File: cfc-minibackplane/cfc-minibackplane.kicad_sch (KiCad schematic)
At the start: 33 parts, among them J1 m55-6001642, J2 Harwin M80-5400442, J3 PI 1792627 + PI 1861690, J4 ORESAT-DEBUG-CONNECTOR-ALL, U2 AMS1117-3.3

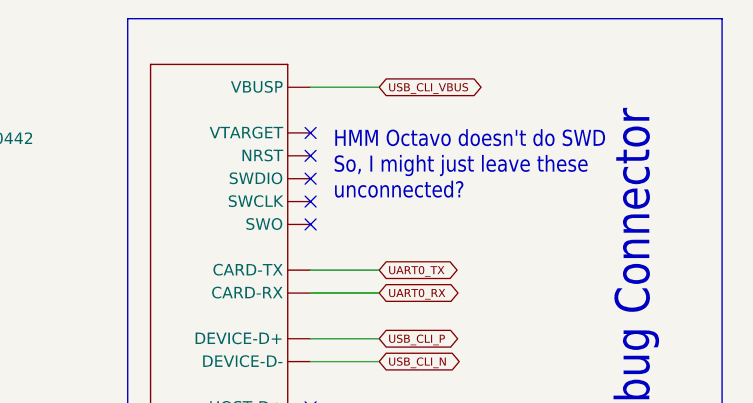
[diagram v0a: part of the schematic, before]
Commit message: Updated 3d models
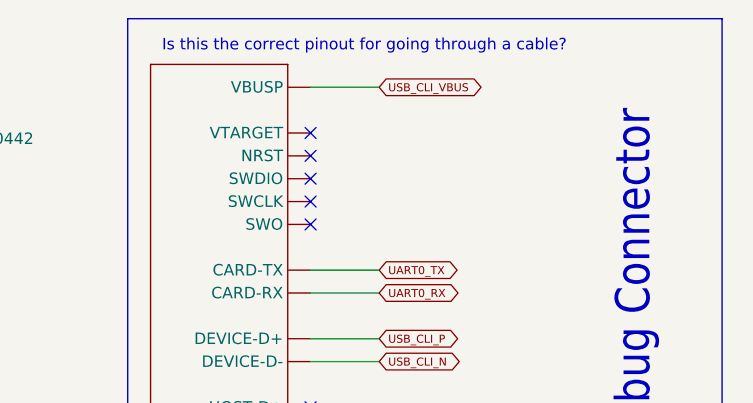
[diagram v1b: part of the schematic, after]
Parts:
- C1.1, C1.2, C20.1, C20.2: footprint oresat-passives:0603-SMALL -> Capacitor_SMD:C_0603_1608Metric
- R1.1, R1.2, R1.3, R1.4, R2, R20.1, R20.2, R20.3, R20.4, R20.5, R20.6, R3: footprint oresat-passives:0603-SMALL -> Resistor_SMD:R_0603_1608Metric
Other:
- note added: "Is this the correct pinout for going through a cable?"
- note removed: "HMM Octavo doesn't do SWD So, I might just leave these unconnected?"
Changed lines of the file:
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@@
+    (effects (font (size 1.27 1.27)) (justify left bottom))
+  )
+  (text "Is this the correct pinout for going through a cable?"
+    (at 350.52 26.67 0)
     (effects (font (size 1.27 1.27)) (justify left bottom))
   )
@@
   (text "Oresat Debug Connector" (at 405.13 33.02 90)
     (effects (font (size 3.81 3.2385)) (justify right bottom))
-  )
-  (text "HMM Octavo doesn't do SWD\nSo, I might just leave these\nunconnected?"
-    (at 369.57 43.18 0)
-    (effects (font (size 1.778 1.5113)) (justify left bottom))
   )
   (text "Aux connectors" (at 311.15 132.08 0)
@@
       (effects (font (size 1.778 1.5113)) (justify left bottom))
     )
-    (property "Footprint" "oresat-passives:0603-SMALL" (at 204.47 125.73 90)
+    (property "Footprint" "Resistor_SMD:R_0603_1608Metric" (at 204.47 125.73 90)
       (effects (font (size 1.27 1.27)) hide)
     )
@@
       (effects (font (size 1.778 1.5113)) (justify left bottom))
     )
-    (property "Footprint" "oresat-passives:0603-SMALL" (at 269.24 171.45 90)
+    (property "Footprint" "Resistor_SMD:R_0603_1608Metric" (at 269.24 171.45 90)
       (effects (font (size 1.27 1.27)) hide)
     )
@@
       (effects (font (size 1.778 1.5113)) (justify left bottom))
     )
-    (property "Footprint" "oresat-passives:0603-SMALL" (at 276.86 180.34 0)
+    (property "Footprint" "Capacitor_SMD:C_0603_1608Metric" (at 276.86 180.34 0)
       (effects (font (size 1.27 1.27)) hide)
     )
@@
       (effects (font (size 1.778 1.5113)) (justify left bottom))
     )
-    (property "Footprint" "oresat-passives:0603-SMALL" (at 204.47 130.81 90)
+    (property "Footprint" "Resistor_SMD:R_0603_1608Metric" (at 204.47 130.81 90)
       (effects (font (size 1.27 1.27)) hide)
     )
@@
       (effects (font (size 1.778 1.5113)) (justify left bottom))
     )
-    (property "Footprint" "oresat-passives:0603-SMALL" (at 217.17 134.62 0)
+    (property "Footprint" "Capacitor_SMD:C_0603_1608Metric" (at 217.17 134.62 0)
       (effects (font (size 1.27 1.27)) hide)
     )
@@
       (effects (font (size 1.27 1.27)))
     )
-    (property "Footprint" "oresat-passives:0603-SMALL" (at 71.12 123.698 90)
+    (property "Footprint" "Resistor_SMD:R_0603_1608Metric" (at 71.12 123.698 90)
       (effects (font (size 1.27 1.27)) hide)
     )
@@
       (effects (font (size 1.778 1.5113)) (justify left bottom))
     )
-    (property "Footprint" "oresat-passives:0603-SMALL" (at 269.24 166.37 90)
+    (property "Footprint" "Resistor_SMD:R_0603_1608Metric" (at 269.24 166.37 90)
       (effects (font (size 1.27 1.27)) hide)
     )
@@
       (effects (font (size 1.778 1.5113)) (justify left bottom))
     )
-    (property "Footprint" "oresat-passives:0603-SMALL" (at 264.16 194.31 90)
+    (property "Footprint" "Resistor_SMD:R_0603_1608Metric" (at 264.16 194.31 90)
       (effects (font (size 1.27 1.27)) hide)
     )
@@
       (effects (font (size 1.778 1.5113)) (justify left bottom))
     )
-    (property "Footprint" "oresat-passives:0603-SMALL" (at 269.24 130.81 90)
+    (property "Footprint" "Resistor_SMD:R_0603_1608Metric" (at 269.24 130.81 90)
       (effects (font (size 1.27 1.27)) hide)
     )
@@
       (effects (font (size 1.778 1.5113)) (justify left bottom))
     )
-    (property "Footprint" "oresat-passives:0603-SMALL" (at 207.01 166.37 90)
+    (property "Footprint" "Resistor_SMD:R_0603_1608Metric" (at 207.01 166.37 90)
       (effects (font (size 1.27 1.27)) hide)
     )
@@
       (effects (font (size 1.778 1.5113)) (justify left bottom))
     )
-    (property "Footprint" "oresat-passives:0603-SMALL" (at 264.16 201.93 90)
+    (property "Footprint" "Resistor_SMD:R_0603_1608Metric" (at 264.16 201.93 90)
       (effects (font (size 1.27 1.27)) hide)
     )
@@
       (effects (font (size 1.778 1.5113)) (justify left bottom))
     )
-    (property "Footprint" "oresat-passives:0603-SMALL" (at 276.86 138.43 0)
+    (property "Footprint" "Capacitor_SMD:C_0603_1608Metric" (at 276.86 138.43 0)
       (effects (font (size 1.27 1.27)) hide)
     )
@@
       (effects (font (size 1.778 1.5113)) (justify left bottom))
     )
-    (property "Footprint" "oresat-passives:0603-SMALL" (at 207.01 171.45 90)
+    (property "Footprint" "Resistor_SMD:R_0603_1608Metric" (at 207.01 171.45 90)
       (effects (font (size 1.27 1.27)) hide)
     )
@@
       (effects (font (size 1.778 1.5113)) (justify left bottom))
     )
-    (property "Footprint" "oresat-passives:0603-SMALL" (at 269.24 125.73 90)
+    (property "Footprint" "Resistor_SMD:R_0603_1608Metric" (at 269.24 125.73 90)
       (effects (font (size 1.27 1.27)) hide)
     )
@@
       (effects (font (size 1.27 1.27)))
     )
-    (property "Footprint" "oresat-passives:0603-SMALL" (at 71.12 126.238 90)
+    (property "Footprint" "Resistor_SMD:R_0603_1608Metric" (at 71.12 126.238 90)
       (effects (font (size 1.27 1.27)) hide)
     )
@@
       (effects (font (size 1.778 1.5113)) (justify left bottom))
     )
-    (property "Footprint" "oresat-passives:0603-SMALL" (at 219.71 175.26 0)
-      (effects (font (size 1.27 1.27)) hide)
-    )
+    (property "Footprint" "Capacitor_SMD:C_0603_1608Metric" (at 219.71 175.26 0)
+      (effects (font (size 1.27 1.27)) hide)
+    )

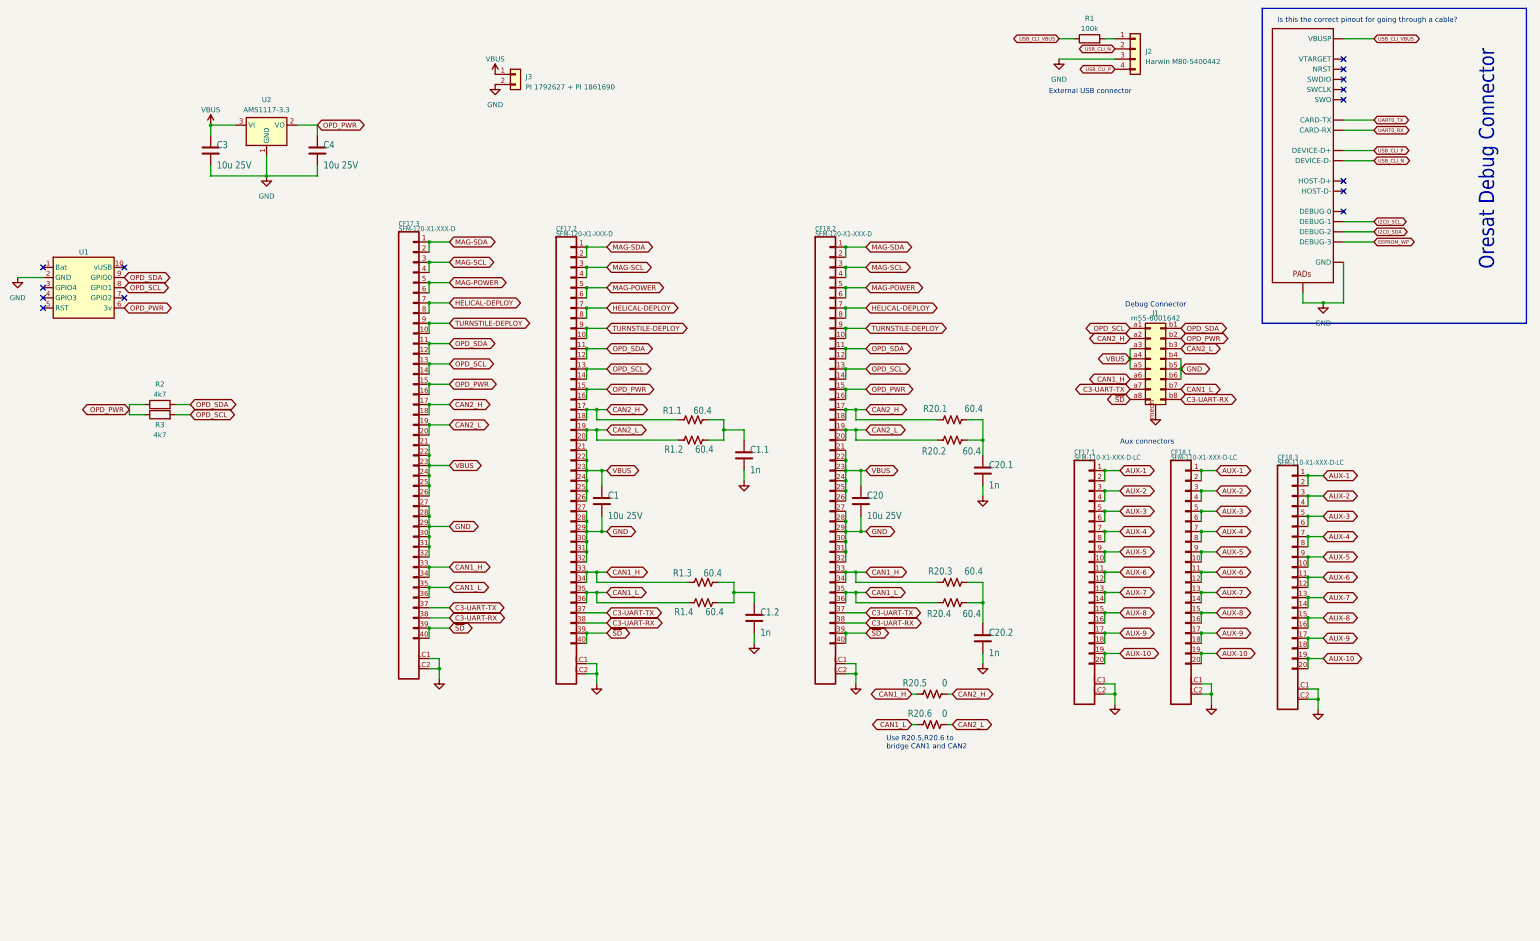
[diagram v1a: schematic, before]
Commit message: Cleaned up schematic and silkscreen
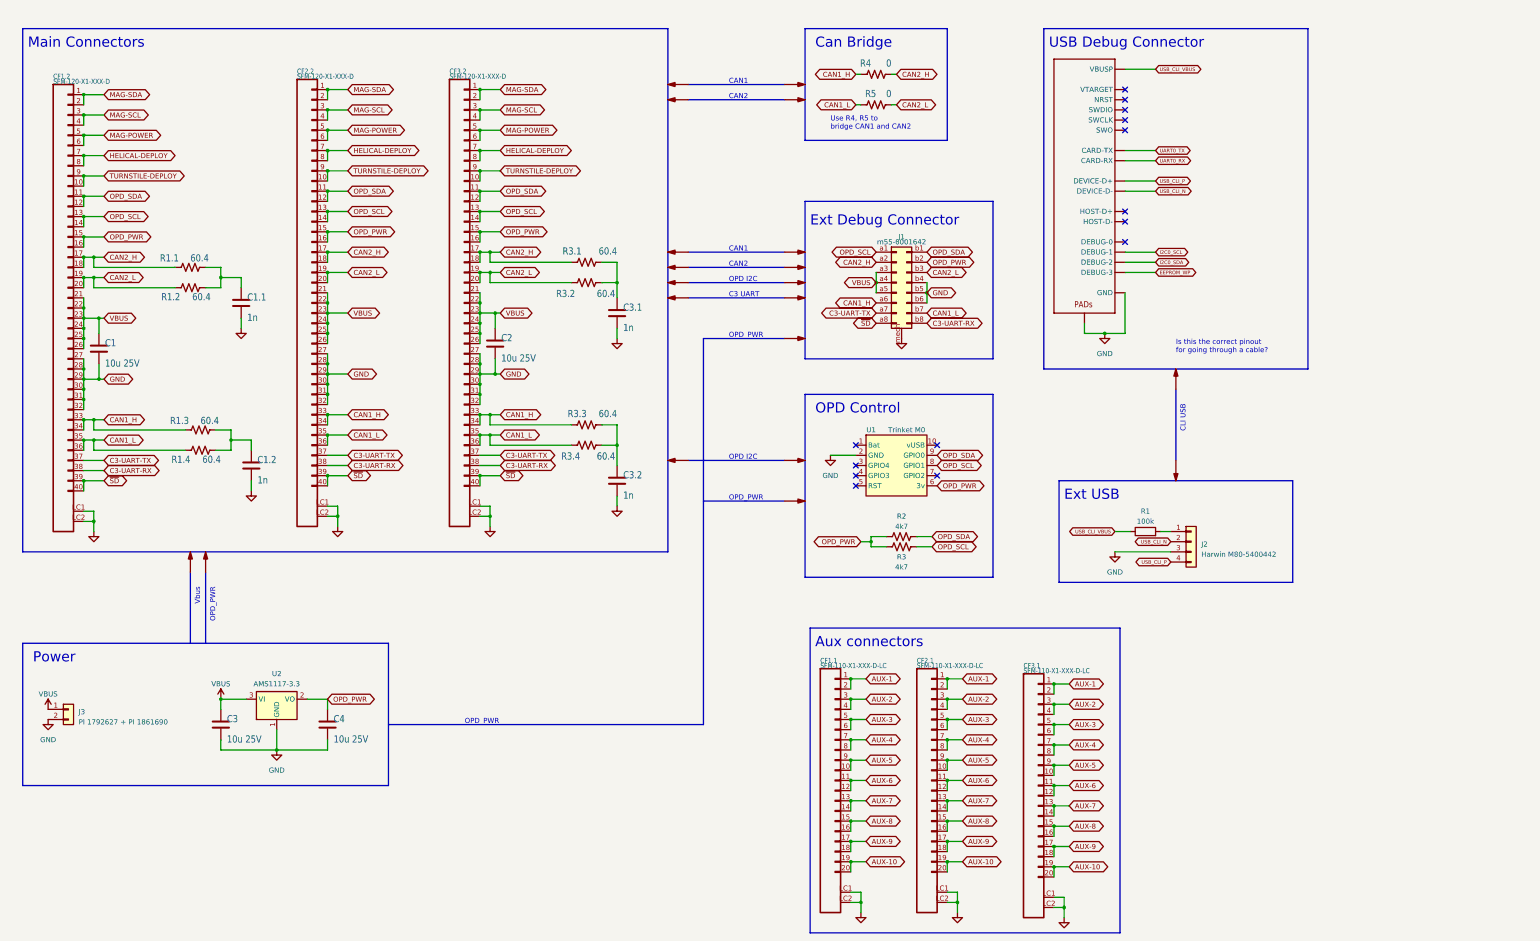
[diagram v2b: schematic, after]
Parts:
- R2, R3: symbol Device:R -> Device:R_US
- U1: value ~ -> Trinket M0
- renumbered C20 to C2, C20.1 to C3.1, C20.2 to C3.2, CF17.1 to CF1.1, CF17.2 to CF1.2, CF18.1 to CF2.1, CF17.3 to CF2.2, CF18.3 to CF3.1, CF18.2 to CF3.2, R20.1 to R3.1, R20.2 to R3.2, R20.3 to R3.3, R20.4 to R3.4, R20.5 to R4, R20.6 to R5
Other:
- note added: "C3 UART"
- note added: "CAN1"
- note added: "CAN2"
- note added: "CLI USB"
- note added: "Can Bridge"
- note added: "Ext Debug Connector"
- note added: "Ext USB"
- note added: "Main Connectors"
- note added: "OPD Control"
- note added: "OPD I2C"
- note added: "OPD_PWR"
- note added: "Power"
- note added: "USB Debug Connector"
- note added: "Use R4, R5 to bridge CAN1 and CAN2"
- note added: "Vbus"
- note removed: "Debug Connector"
- note removed: "External USB connector"
- note removed: "Oresat Debug Connector"
- note removed: "Use R20.5,R20.6 to bridge CAN1 and CAN2"
- title: (none) -> OreSat Mini Backplane
- moved on the sheet: C1, C1.1, C1.2, C2, C3, C3.1, C3.2, C4, CF1.1, CF1.2, CF2.1, CF2.2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

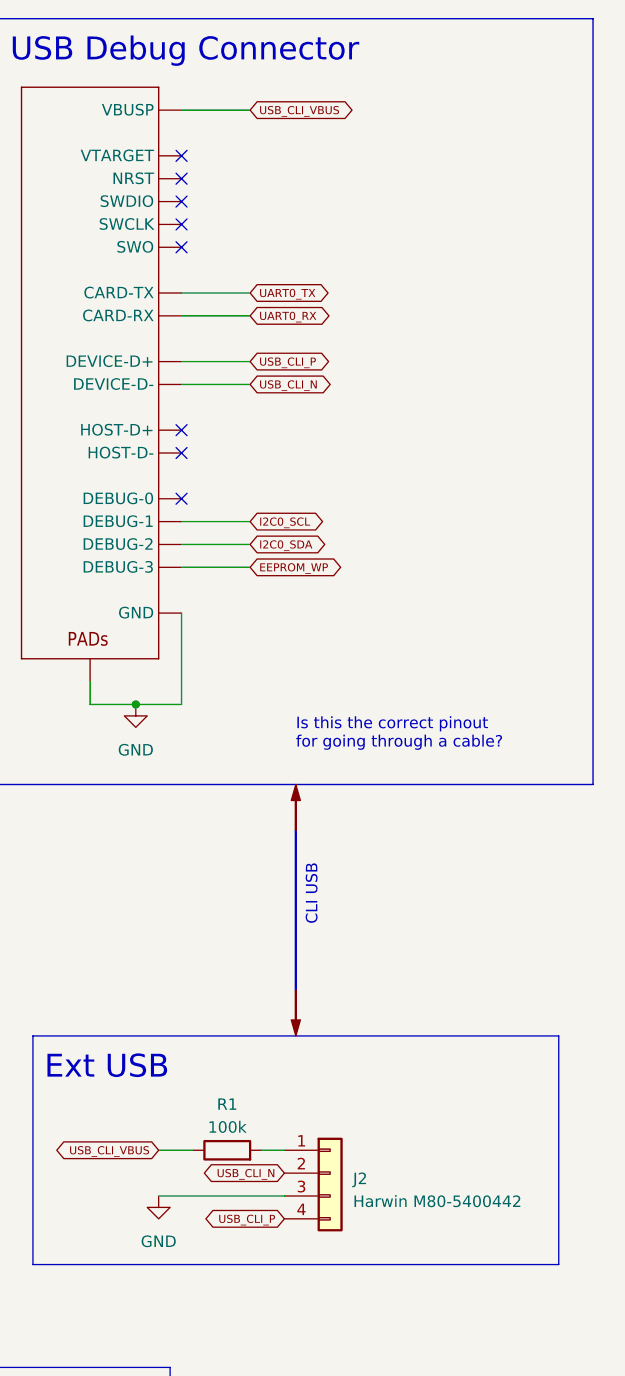
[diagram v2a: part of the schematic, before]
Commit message: Updated board based on CFC meeting
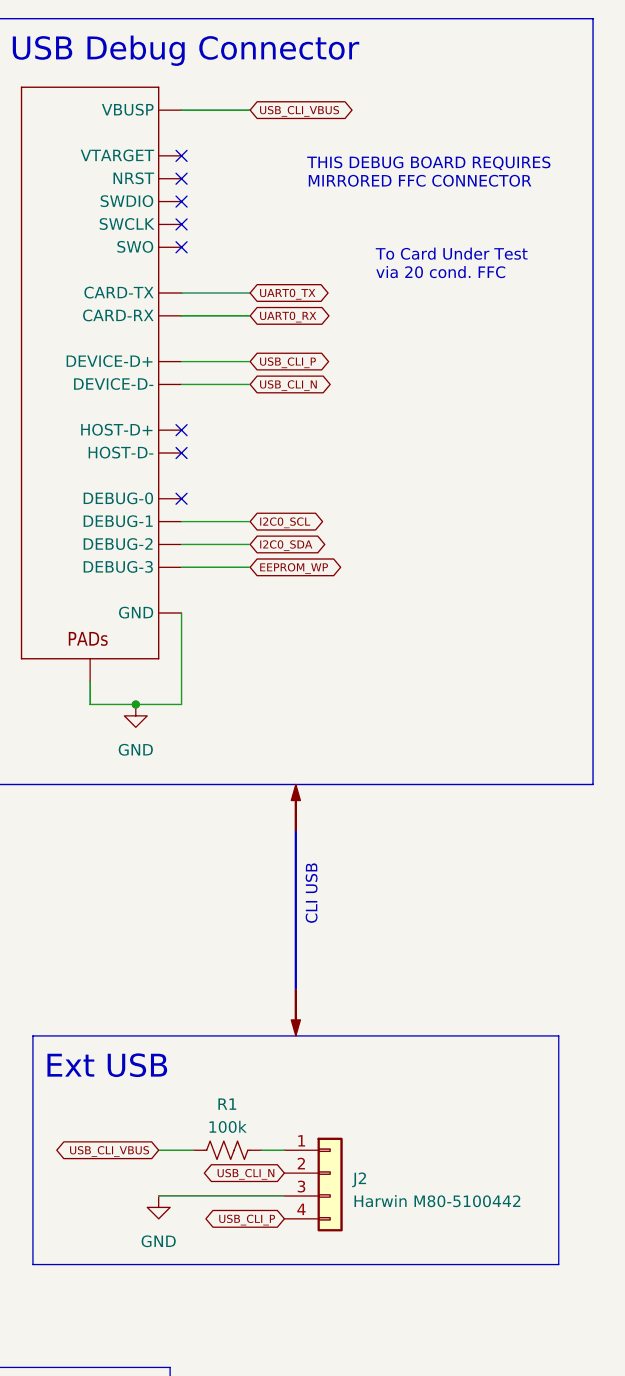
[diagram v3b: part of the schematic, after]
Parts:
- J2: value Harwin M80-5400442 -> Harwin M80-5100442; footprint oresat-connectors:J-Harwin-M80-5400442 -> oresat-connectors:J-Harwin-M80-5100442; DPN (none) -> 952-2343-ND; MPN (none) -> M80-5100442
- J3: footprint Connector_Phoenix_MSTB:PhoenixContact_MSTB_2,5_2-GF-5,08_1x02_P5.08mm_Horizontal_ThreadedFlange_MountHole -> Connector_Phoenix_MSTB:PhoenixContact_MSTBV_2,5_2-GF_1x02_P5.00mm_Vertical_ThreadedFlange_MountHole
- J4: footprint oresat-connectors:J-TE_2-1734592-0 -> oresat-connectors:J-TE_2-1734592-0_FFC_MIRRORED
- R1: footprint Resistor_SMD:R_1206_3216Metric -> Resistor_SMD:R_0603_1608Metric; symbol Device:R -> Device:R_US
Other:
- note added: "THIS DEBUG BOARD REQUIRES MIRRORED FFC CONNECTOR"
- note added: "To Card Under Test via 20 cond. FFC"
- note removed: "Is this the correct pinout for going through a cable?"

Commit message: Updated BOM
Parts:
- added J3.1: PC 1861690, symbol Graphic:SYM_Flash_Small
- C1, C2, C3, C4: DPN (none) -> GCM31CC71E106KA03K; MPN (none) -> 490-14533-1-ND
- C1.1, C1.2, C3.1, C3.2: DPN (none) -> 399-C0603C102F1GACAUTOCT-ND; MPN (none) -> GCM1885C2A102JA16D
- CF1.1, CF2.1, CF3.1: DPN (none) -> SFM-110-01-L-D-LC-ND; MPN (none) -> SFM-110-01-L-D-LC
- CF1.2, CF2.2, CF3.2: DPN (none) -> SFM-120-01-L-D-LC-ND; MPN (none) -> SFM-120-01-L-D-LC
- J1: DPN (none) -> M55-6001642R; MPN (none) -> 952-3836-1-ND
- J3: value PI 1792627 + PI 1861690 -> PC 180926; DPN (none) -> 277-2619-ND; MPN (none) -> 1809267
- J4: DPN (none) -> A100287CT-ND; MPN (none) -> 2-1734592-0
- R1: DPN (none) -> RHM100KAFCT-ND; MPN (none) -> ESR18EZPF1003
- R1.1, R1.2, R1.3, R1.4, R3.1, R3.2, R3.3, R3.4: footprint Resistor_SMD:R_0603_1608Metric -> Resistor_SMD:R_1206_3216Metric; DPN (none) -> RHM60.4AFCT-ND; MPN (none) -> ESR18EZPF60R4
- R2, R3: DPN (none) -> RMCF0603FT4K70CT-ND; MPN (none) -> RMCF0603FT4K70
- R4, R5: DPN (none) -> RMCF0603ZT0R00CT-ND; MPN (none) -> RMCF0603ZT0R00
- U1: DPN (none) -> 1528-2361-ND; MPN (none) -> 3500
- U2: DPN (none) -> 4518-AMS1117-3.3CT-ND; MPN (none) -> AMS1117-3.3
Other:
- note added: "Power Plug"

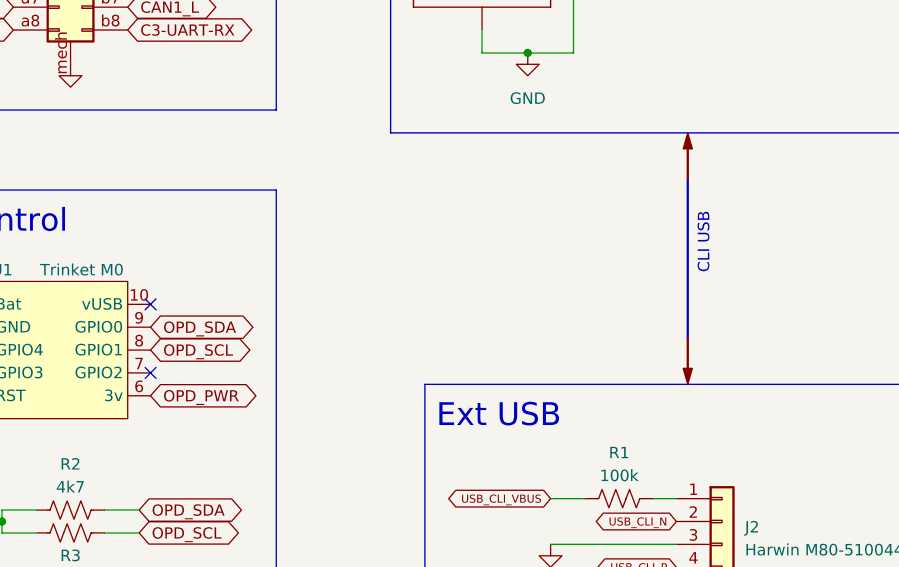
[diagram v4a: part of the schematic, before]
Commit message: Added not on Trinket wiring bug.
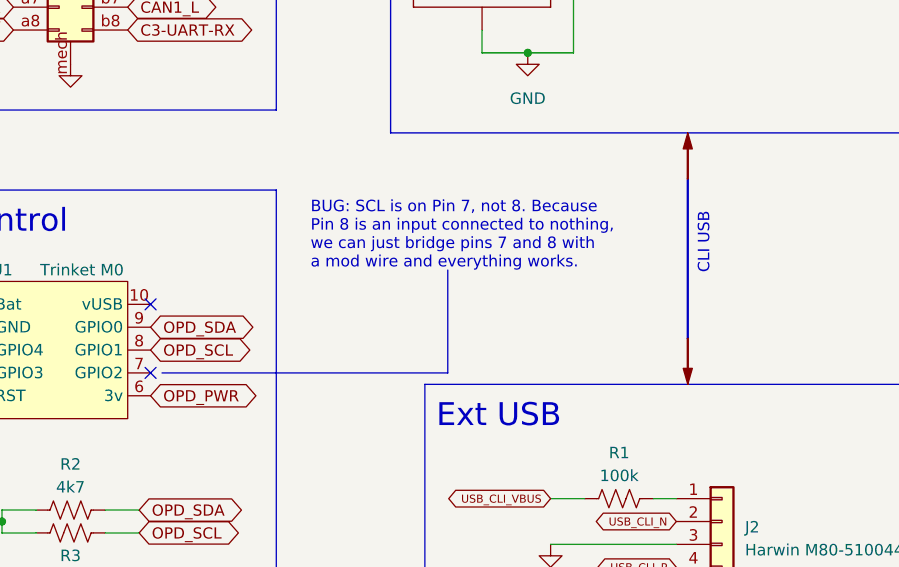
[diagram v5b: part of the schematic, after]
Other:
- note added: "BUG: SCL is on Pin 7, not 8. Because Pin 8 is an input connected to nothing, we can just bridge pins 7 and 8 with a mod wire and everything works."
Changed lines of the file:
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@@
     (stroke (width 0) (type default))
+  )
+  (polyline (pts (xy 298.45 128.27) (xy 298.45 139.7))
+    (stroke (width 0) (type default) (color 255 0 0 1))
   )
   (wire (pts (xy 57.15 69.85) (xy 52.07 69.85))
@@
   (wire (pts (xy 297.18 250.19) (xy 297.18 247.65))
     (stroke (width 0) (type default))
+  )
+  (polyline (pts (xy 266.7 139.7) (xy 298.45 139.7))
+    (stroke (width 0) (type default) (color 255 0 0 1))
   )
   (wire (pts (xy 243.84 236.22) (xy 243.84 238.76))
@@
     (effects (font (size 2.54 2.54)) (justify left bottom))
   )
+  (text "BUG: SCL is on Pin 7, not 8. Because\nPin 8 is an input connected to nothing,\nwe can just bridge pins 7 and 8 with \na mod wire and everything works."
+    (at 283.21 128.27 0)
+    (effects (font (size 1.27 1.27) (color 255 0 0 1)) (justify left bottom))
+  )
   (text "OPD_PWR" (at 147.32 201.93 0)
